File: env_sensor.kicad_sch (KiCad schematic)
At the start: 25 parts, among them J1 E Paper, J10 Conn_01x06_Pin, J2 5V_in, J3 Barrel_Jack, J4 LED_OUTPUT, J5 Conn_01x02_Pin, J6 Conn_01x04_Socket, J8 v5_v3, Q1 NMOS, Q2 NMOS, Q3 NMOS, U1 ESP32-DevKitC, U1 MH-Z19B, U4 TXB0104PW, U5 BME280

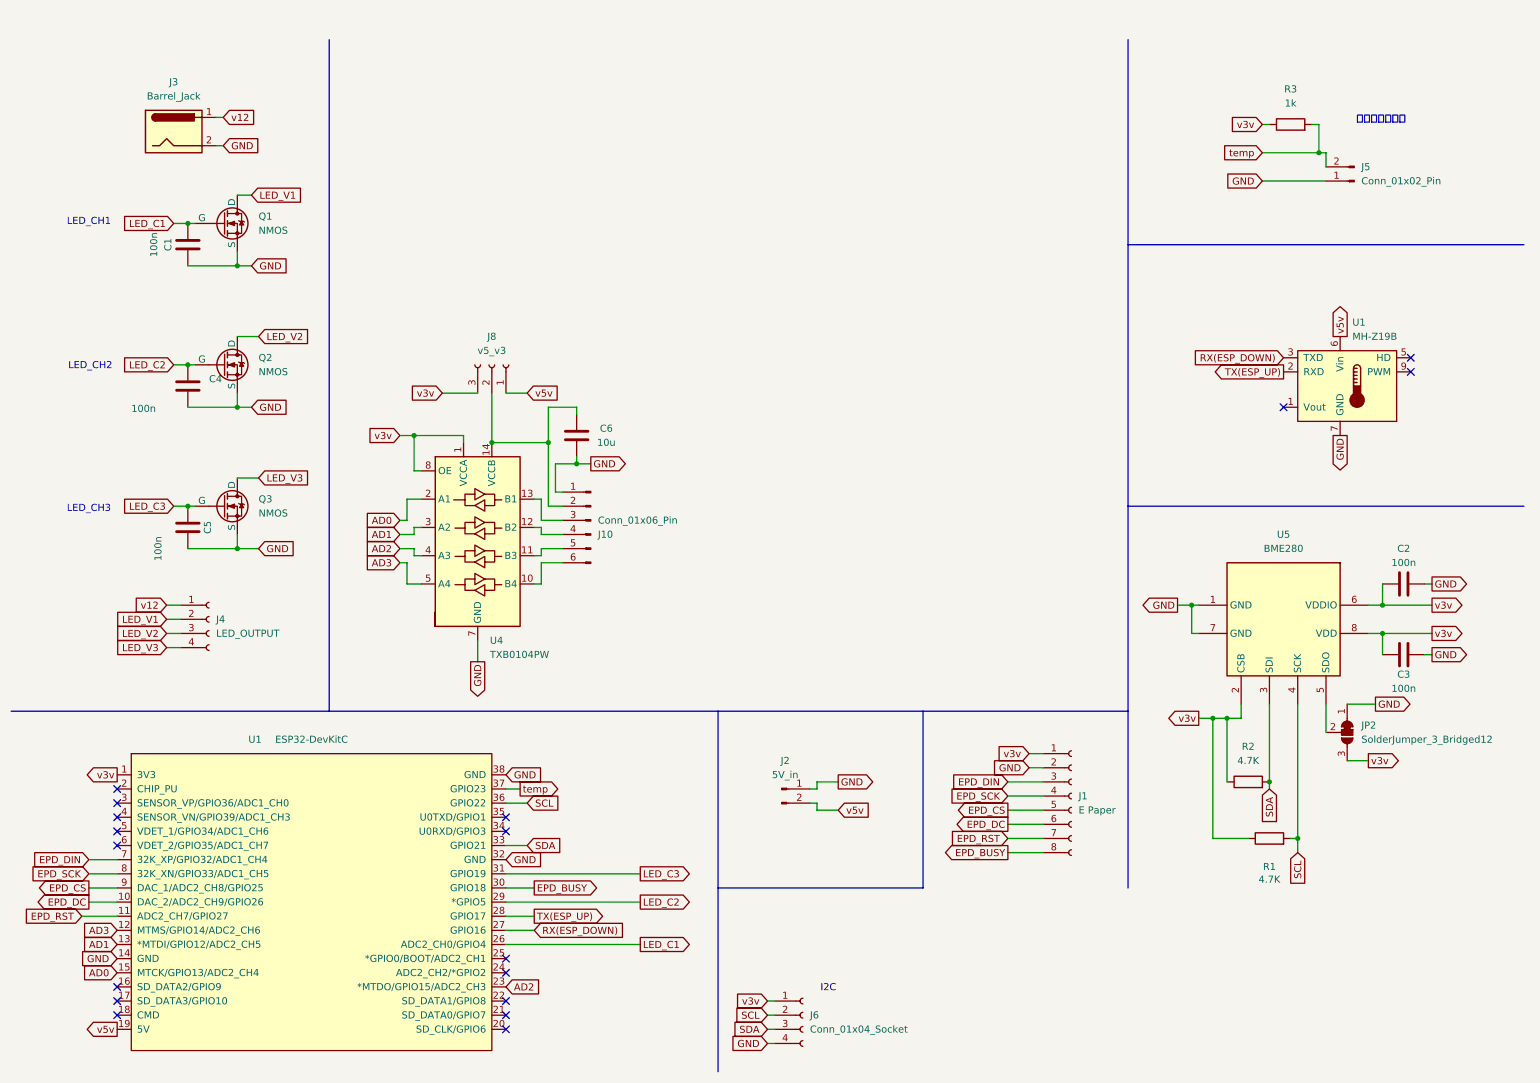
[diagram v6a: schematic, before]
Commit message: add esp32_s3
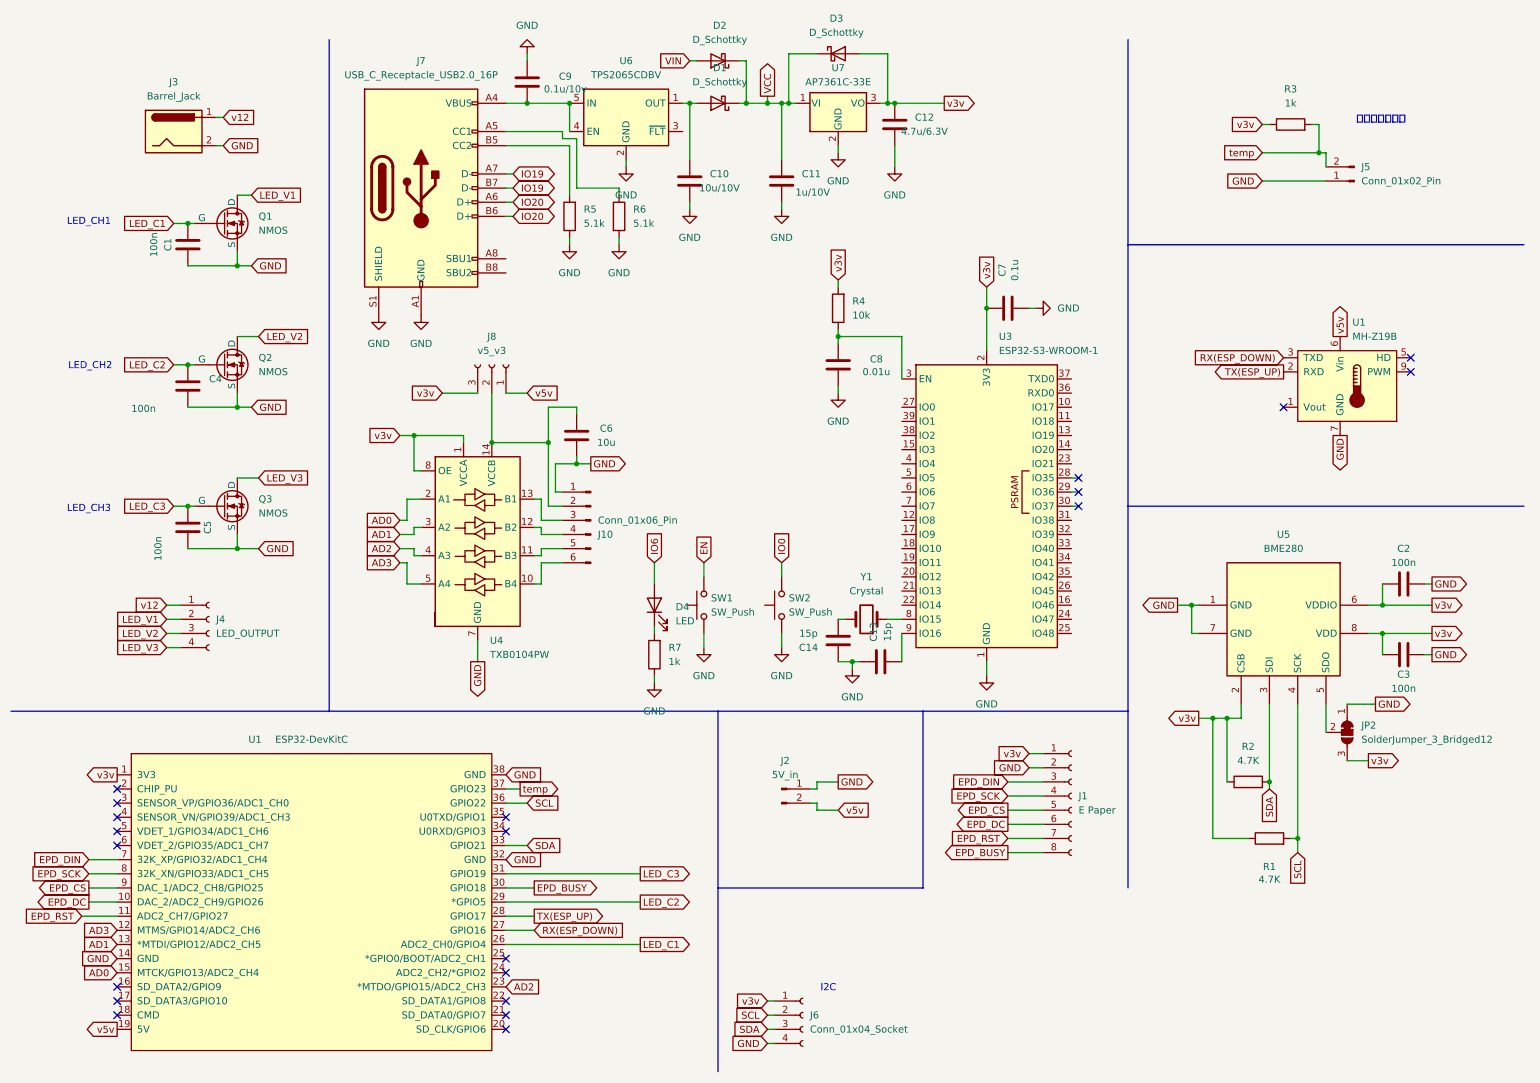
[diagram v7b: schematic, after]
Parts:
- added C10: 10u/10V, Capacitor_SMD:C_0603_1608Metric, symbol Device:C
- added C11: 1u/10V, Capacitor_SMD:C_0603_1608Metric, symbol Device:C
- added C12: 4.7u/6.3V, Capacitor_SMD:C_0603_1608Metric, symbol Device:C
- added C13, C14: 15p, Capacitor_SMD:C_0603_1608Metric, symbol Device:C
- added C7: 0.1u, Capacitor_SMD:C_0603_1608Metric, symbol Device:C
- added C8: 0.01u, Capacitor_SMD:C_0603_1608Metric, symbol Device:C
- added C9: 0.1u/10v, Capacitor_SMD:C_0603_1608Metric, symbol Device:C
- added D1, D2, D3: D_Schottky, symbol Device:D_Schottky
- added D4: LED, symbol Device:LED
- added J7: USB_C_Receptacle_USB2.0_16P, symbol Connector:USB_C_Receptacle_USB2.0_16P
- added R4: 10k, Resistor_SMD:R_0603_1608Metric, symbol Device:R
- added R5, R6: 5.1k, Resistor_SMD:R_0603_1608Metric, symbol Device:R
- added R7: 1k, Resistor_SMD:R_0603_1608Metric, symbol Device:R
- added SW1, SW2: SW_Push, symbol Switch:SW_Push
- added U3: ESP32-S3-WROOM-1, RF_Module:ESP32-S3-WROOM-1, symbol RF_Module:ESP32-S3-WROOM-1
- added U6: TPS2065CDBV, Package_TO_SOT_SMD:SOT-23-5, symbol Power_Management:TPS2065CDBV
- added U7: AP7361C-33E, Package_TO_SOT_SMD:SOT-223-3_TabPin2, symbol Regulator_Linear:AP7361C-33E
- added Y1: Crystal, Crystal:Crystal_SMD_3215-2Pin_3.2x1.5mm, symbol Device:Crystal
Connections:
- net GND: now also C10.2, C11.2, C12.2, C13.1, C14.1, C7.2, C8.2, C9.1, J7.A1 (GND), J7.A12 (GND), J7.B1 (GND), J7.B12 (GND), J7.S1 (SHIELD), R5.1, R6.2, R7.1, SW1.1, SW2.1, U3.1 (GND), U3.40 (GND), U3.41 (GND), U6.2 (GND), U7.2 (GND)
- net v3v: now also C12.1, C7.1, D3.2 (A), R4.2, U3.2 (3V3), U7.3 (VO)
- new net: D4.1 (K), R7.2
- new net: C8.1, R4.1, U3.3 (EN)
- new net: U3.8 (IO15), Y1.1
- new net: C13.2, U3.9 (IO16)
- new net: C14.2, Y1.2
- new net: C9.2, J7.A4 (VBUS), J7.A9 (VBUS), J7.B4 (VBUS), J7.B9 (VBUS), U6.4 (EN), U6.5 (IN)
- new net: J7.B5 (CC2), R5.2
- new net: C10.1, D1.2 (A), U6.1 (OUT)
- new net: J7.A5 (CC1), R6.1
- new net EN: SW1.2
- new net IO0: SW2.2
- new net IO19: J7.A7 (D-), J7.B7 (D-)
- new net IO20: J7.A6 (D+), J7.B6 (D+)
- new net IO6: D4.2 (A)
- new net VCC: C11.1, D1.1 (K), D2.1 (K), D3.1 (K), U7.1 (VI)
- new net VIN: D2.2 (A)
- no-connect marks 18 -> 21

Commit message: update
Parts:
- removed J2: 5V_in, Connector_PinSocket_2.54mm:PinSocket_1x02_P2.54mm_Vertical, symbol Connector:Conn_01x02_Pin
- removed U1: ESP32-DevKitC, Espressif:ESP32-DevKitC, symbol ESP32:ESP32-DevKitC
- added J9: DEBUG, Connector_PinSocket_2.54mm:PinSocket_1x05_P2.54mm_Vertical, symbol Connector:Conn_01x05_Socket
- D1, D2, D3: footprint (none) -> Diode_SMD:D_SMA; LCSC (none) -> C86598
- D4: value LED -> POWER; footprint (none) -> LED_SMD:LED_0603_1608Metric; LCSC (none) -> C3030991
- J10: value Conn_01x06_Pin -> PWMOUT
- J5: value Conn_01x02_Pin -> RegSense
- J6: value Conn_01x04_Socket -> I2c
- J7: footprint (none) -> Connector_USB:USB_C_Receptacle_GCT_USB4105-xx-A_16P_TopMnt_Horizontal
- JP2: value SolderJumper_3_Bridged12 -> Default77
- SW1: value SW_Push -> EN; LCSC (none) -> C2844396
- SW2: value SW_Push -> BOOT; LCSC (none) -> C2844396
- U1: footprint sensor_Carbon_dioxide:mh-z19b -> mh-z19b:Winsen_MH-Z19B
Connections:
- net EPD_BUSY is gone; now on net EPD_BackLight: J1.8 (Pin_8)
- net EPD_CS is gone; now on net EPD_ChipSelect: J1.5 (Pin_5)
- net EPD_DC is gone; now on net EPD_DataControl: J1.6 (Pin_6)
- net EPD_DIN is gone; now on net SPI_MOSI: J1.3 (Pin_3)
- net EPD_SCK is gone; now on net SPI_SCLK: J1.4 (Pin_4)
- net VIN is gone; now on net v5v: D2.2 (A)
- net AD0: now also U3.23 (IO21)
- net AD1: now also U3.24 (IO47)
- net AD2: now also U3.25 (IO48)
- net AD3: now also U3.26 (IO45)
- net EN: now also C8.1, R4.1, U3.3 (EN)
- net EPD_RST: now also U3.21 (IO13)
- net GND: now also J9.1 (Pin_1)
- net IO0: now also U3.27 (IO0)
- net IO19: now also U3.13 (IO19)
- net IO20: now also U3.14 (IO20)
- net IO6: now also U3.6 (IO6)
- net LED_C1: now also U3.12 (IO8)
- net LED_C2: now also U3.10 (IO17)
- net LED_C3: now also U3.11 (IO18)
- net RX(ESP_DOWN): now also U1.2 (RXD), U3.4 (IO4); no longer U1.3 (TXD)
- net SCL: now also U3.15 (IO3)
- net SDA: now also U3.16 (IO46)
- net TX(ESP_UP): now also U1.3 (TXD), U3.5 (IO5); no longer U1.2 (RXD)
- net temp: now also U3.39 (IO1)
- net SPI_MOSI: now reaches U3.17 (IO9)
- net SPI_SCLK: now reaches U3.18 (IO10)
- net EPD_ChipSelect: now reaches U3.19 (IO11)
- net EPD_DataControl: now reaches U3.20 (IO12)
- net EPD_BackLight: now reaches U3.22 (IO14)
- net DEBUG_TCK: now reaches U3.32 (IO39)
- net DEBUG_TCK: now also J9.5 (Pin_5)
- net DEBUG_TDO: now reaches U3.33 (IO40)
- net DEBUG_TDO: now also J9.4 (Pin_4)
- net DEBUG_TDI: now reaches U3.34 (IO41)
- net DEBUG_TDI: now also J9.3 (Pin_3)
- net DEBUG_TMS: now reaches U3.35 (IO42)
- net DEBUG_TMS: now also J9.2 (Pin_2)
- no-connect marks 21 -> 6
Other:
- moved on the sheet: C13, C14, C8, SW2, Y1
